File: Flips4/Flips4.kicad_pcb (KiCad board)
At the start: 2 copper layers, 21 x 59.1 mm, 7 parts, among them CN1 UFP2810, CN2 Conn_02x16_Counter_Clockwise, U1 FP2800A

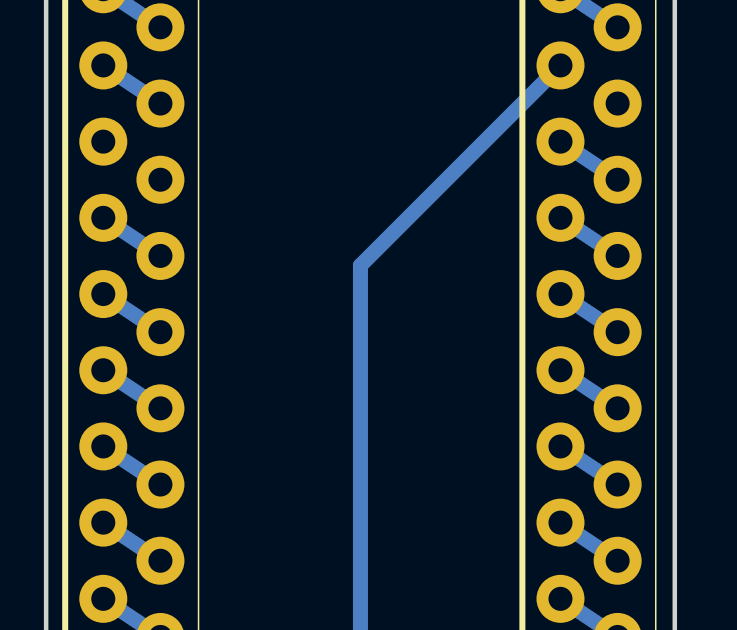
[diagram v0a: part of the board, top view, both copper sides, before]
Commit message: toggling copper behind "K" of "KiCad" logo
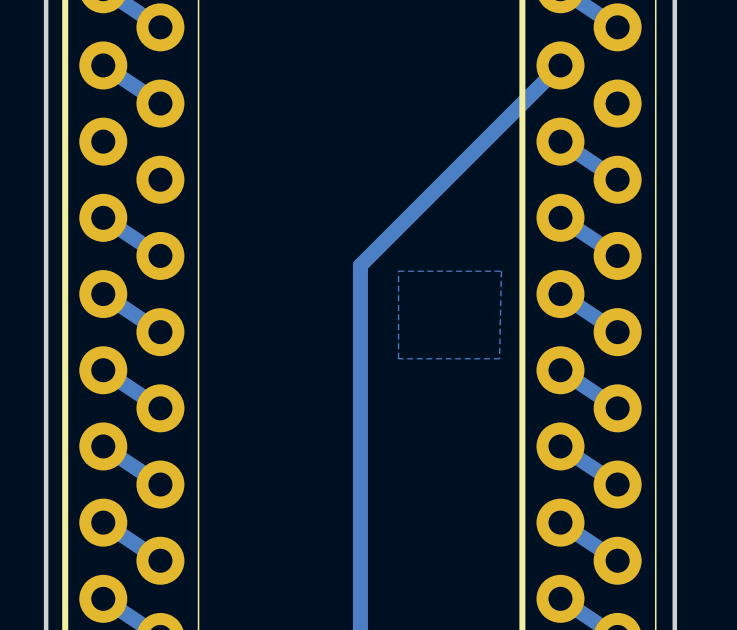
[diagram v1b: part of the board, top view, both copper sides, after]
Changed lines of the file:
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@@
+    )
+  )
+  (zone (net 0) (net_name "") (layer B.Cu) (hatch edge 0.508)
+    (connect_pads (clearance 0.1524))
+    (min_thickness 0.254)
+    (fill yes (arc_segments 16) (thermal_gap 0.508) (thermal_bridge_width 0.508))
+    (polygon
+      (pts
+        (xy 230.1875 86.233) (xy 233.6165 86.233) (xy 233.553 89.154) (xy 230.1875 89.154)
+      )
     )
   )

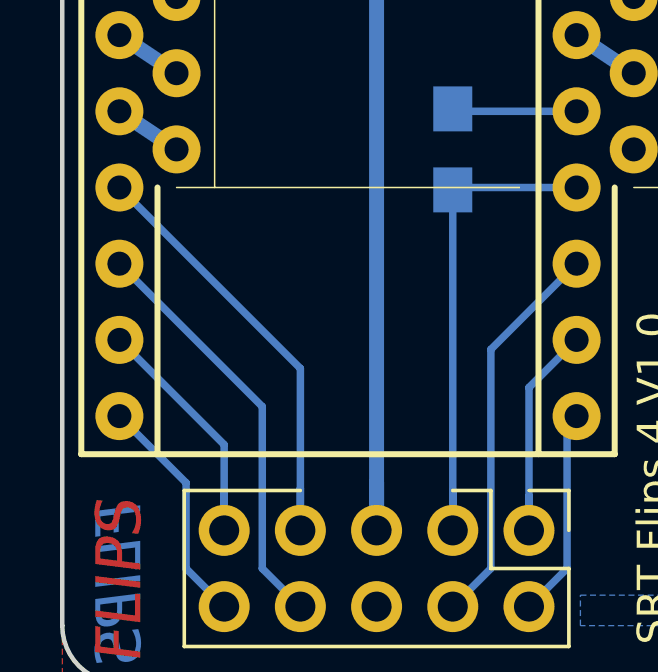
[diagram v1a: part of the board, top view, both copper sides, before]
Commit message: adding bypass capacitors
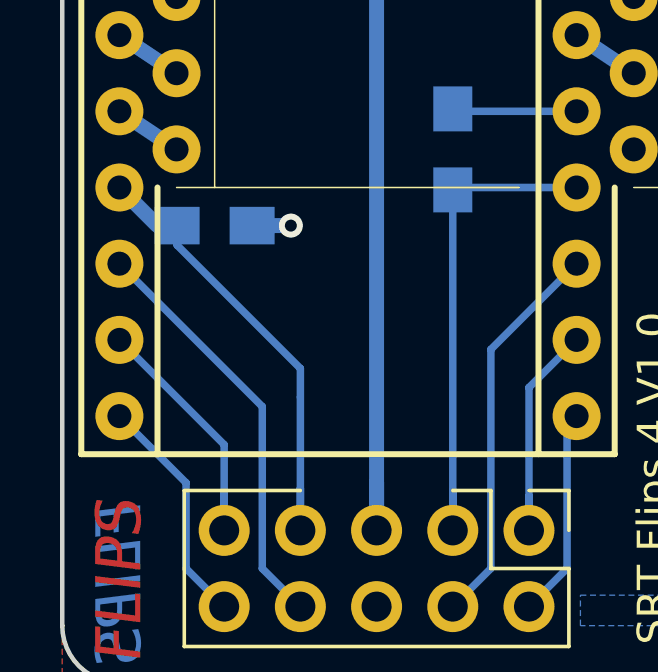
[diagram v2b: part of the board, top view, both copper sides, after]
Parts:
- added C1: 0U1, Capacitors_SMD:C_0805_HandSoldering, B.Cu at (223.5, 108.6)
- R1: value 10K/OPT -> 10K
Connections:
- CN2 pad 17: (no net) -> Net-(CN2-Pad17)
- CN2 pad 27: (no net) -> Net-(CN2-Pad27)
- CN2 pad 7: (no net) -> Net-(CN2-Pad7)
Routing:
- net GND: track 4.16 -> 5.45 mm, vias 0 -> 1
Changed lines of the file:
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@@
     (thickness 1.6)
     (drawings 35)
-    (tracks 64)
+    (tracks 70)
     (zones 0)
-    (modules 7)
-    (nets 40)
+    (modules 8)
+    (nets 43)
   )
   (page A4)
@@
   )
   (layers
-    (0 F.Cu signal hide)
+    (0 F.Cu signal)
     (31 B.Cu signal)
     (32 B.Adhes user)
@@
   (net 38 /A2)
   (net 39 /A0)
+  (net 40 "Net-(CN2-Pad27)")
+  (net 41 "Net-(CN2-Pad7)")
+  (net 42 "Net-(CN2-Pad17)")
   (net_class Default "Dies ist die voreingestellte Netzklasse."
     (clearance 0.2)
@@
     (add_net /Data)
     (add_net /Enable)
+    (add_net "Net-(CN2-Pad17)")
+    (add_net "Net-(CN2-Pad27)")
+    (add_net "Net-(CN2-Pad7)")
     (add_net VCC)
   )
@@
     (add_net "Net-(CN2-Pad8)")
     (add_net "Net-(CN2-Pad9)")
+  )
+  (module Capacitors_SMD:C_0805_HandSoldering (layer B.Cu)
+    (at 223.52 108.585)
+    (descr "Capacitor SMD 0805, hand soldering")
+    (tags "capacitor 0805")
+    (attr smd)
+    (fp_text reference C1 (at 0.635 2.54 90) (layer B.SilkS)
+      (effects (font (size 1 1) (thickness 0.15)) (justify mirror))
+    )
+    (fp_text value 0U1 (at -0.635 2.54 90) (layer B.SilkS)
+      (effects (font (size 1 1) (thickness 0.15)) (justify mirror))
+    )
+    (fp_line (start 2.25 -0.87) (end -2.25 -0.87) (layer B.CrtYd) (width 0.05))
+    (fp_line (start 2.25 -0.87) (end 2.25 0.88) (layer B.CrtYd) (width 0.05))
+    (fp_line (start -2.25 0.88) (end -2.25 -0.87) (layer B.CrtYd) (width 0.05))
+    (fp_line (start -2.25 0.88) (end 2.25 0.88) (layer B.CrtYd) (width 0.05))
+    (fp_line (start -0.5 -0.85) (end 0.5 -0.85) (layer B.SilkS) (width 0.12))
+    (fp_line (start 0.5 0.85) (end -0.5 0.85) (layer B.SilkS) (width 0.12))
+    (fp_line (start -1 0.62) (end 1 0.62) (layer B.Fab) (width 0.1))
+    (fp_line (start 1 0.62) (end 1 -0.62) (layer B.Fab) (width 0.1))
+    (fp_line (start 1 -0.62) (end -1 -0.62) (layer B.Fab) (width 0.1))
+    (fp_line (start -1 -0.62) (end -1 0.62) (layer B.Fab) (width 0.1))
+    (fp_text user %R (at 0 1.75) (layer B.Fab)
+      (effects (font (size 1 1) (thickness 0.15)) (justify mirror))
+    )
+    (pad 2 smd rect (at 1.25 0) (size 1.5 1.25) (layers B.Cu B.Paste B.Mask)
+      (net 30 GND))
+    (pad 1 smd rect (at -1.25 0) (size 1.5 1.25) (layers B.Cu B.Paste B.Mask)
+      (net 31 VCC))
+    (model Capacitors_SMD.3dshapes/C_0805.wrl
+      (at (xyz 0 0 0))
+      (scale (xyz 1 1 1))
+      (rotate (xyz 0 0 0))
+    )
   )
   (module Own:Pin_Header_Angle_Shrouded_2x05_Pitch2.54mm (layer F.Cu)
@@
     (pad 12 thru_hole oval (at 0 27.94) (size 1.6 1.6) (drill 0.8) (layers *.Cu *.Mask)
       (net 9 "Net-(CN2-Pad12)"))
-    (pad 27 thru_hole oval (at 15.24 12.7) (size 1.6 1.6) (drill 0.8) (layers *.Cu *.Mask))
+    (pad 27 thru_hole oval (at 15.24 12.7) (size 1.6 1.6) (drill 0.8) (layers *.Cu *.Mask)
+      (net 40 "Net-(CN2-Pad27)"))
     (pad 11 thru_hole oval (at 0 25.4) (size 1.6 1.6) (drill 0.8) (layers *.Cu *.Mask)
       (net 11 "Net-(CN2-Pad11)"))
@@
     (pad 23 thru_hole oval (at 15.24 22.86) (size 1.6 1.6) (drill 0.8) (layers *.Cu *.Mask)
       (net 24 "Net-(CN2-Pad23)"))
-    (pad 7 thru_hole oval (at 0 15.24) (size 1.6 1.6) (drill 0.8) (layers *.Cu *.Mask))
+    (pad 7 thru_hole oval (at 0 15.24) (size 1.6 1.6) (drill 0.8) (layers *.Cu *.Mask)
+      (net 41 "Net-(CN2-Pad7)"))
     (pad 22 thru_hole oval (at 15.24 25.4) (size 1.6 1.6) (drill 0.8) (layers *.Cu *.Mask)
       (net 26 "Net-(CN2-Pad22)"))
@@
     (pad 2 thru_hole oval (at 0 2.54) (size 1.6 1.6) (drill 0.8) (layers *.Cu *.Mask)
       (net 27 "Net-(CN2-Pad2)"))
-    (pad 17 thru_hole oval (at 15.24 38.1) (size 1.6 1.6) (drill 0.8) (layers *.Cu *.Mask))
+    (pad 17 thru_hole oval (at 15.24 38.1) (size 1.6 1.6) (drill 0.8) (layers *.Cu *.Mask)
+      (net 42 "Net-(CN2-Pad17)"))
     (pad 1 thru_hole circle (at 0 0) (size 1.6 1.6) (drill 0.8) (layers *.Cu *.Mask)
       (net 29 "Net-(CN2-Pad1)"))
@@
       (effects (font (size 1 1) (thickness 0.15)) (justify mirror))
     )
-    (fp_text value 10K/OPT (at 0 -1.75 90) (layer B.SilkS)
+    (fp_text value 10K (at 0 -1.75 90) (layer B.SilkS)
       (effects (font (size 1 1) (thickness 0.15)) (justify mirror))
     )
@@
   (segment (start 231.5375 104.775) (end 231.4575 104.695) (width 0.5) (layer B.Cu) (net 30) (status 30))
   (segment (start 235.585 104.775) (end 231.5375 104.775) (width 0.25) (layer B.Cu) (net 30) (status 30))
-  (segment (start 220.345 107.315) (end 226.3775 113.3475) (width 0.25) (layer B.Cu) (net 31) (status 400010))
-  (segment (start 226.3775 113.3475) (end 226.3775 117.348) (width 0.25) (layer B.Cu) (net 31))
+  (via (at 226.06 108.585) (size 0.8) (drill 0.4) (layers F.Cu B.Cu) (net 30))
+  (segment (start 224.77 108.585) (end 226.06 108.585) (width 0.5) (layer B.Cu) (net 30) (status 400010))
   (segment (start 226.3775 117.348) (end 226.3775 118.11) (width 0.25) (layer B.Cu) (net 31) (status 800020))
   (segment (start 226.3775 118.745) (end 226.3775 117.348) (width 0.25) (layer B.Cu) (net 31) (status 400010))
+  (segment (start 226.3775 114.3) (end 226.3775 117.348) (width 0.25) (layer B.Cu) (net 31))
+  (segment (start 222.27 108.585) (end 221.615 108.585) (width 0.25) (layer B.Cu) (net 31) (status C00000))
+  (segment (start 221.615 108.585) (end 220.345 107.315) (width 0.5) (layer B.Cu) (net 31) (status C00000))
+  (segment (start 226.3775 114.3) (end 226.3775 113.3475) (width 0.25) (layer B.Cu) (net 31))
+  (segment (start 226.3775 113.3475) (end 222.27 109.24) (width 0.25) (layer B.Cu) (net 31))
+  (segment (start 222.27 109.24) (end 222.27 108.585) (width 0.25) (layer B.Cu) (net 31) (status 800000))
   (segment (start 235.585 79.375) (end 228.9175 86.0425) (width 0.5) (layer B.Cu) (net 32) (status 10))
   (segment (start 228.9175 86.0425) (end 228.9175 117.1575) (width 0.5) (layer B.Cu) (net 32))

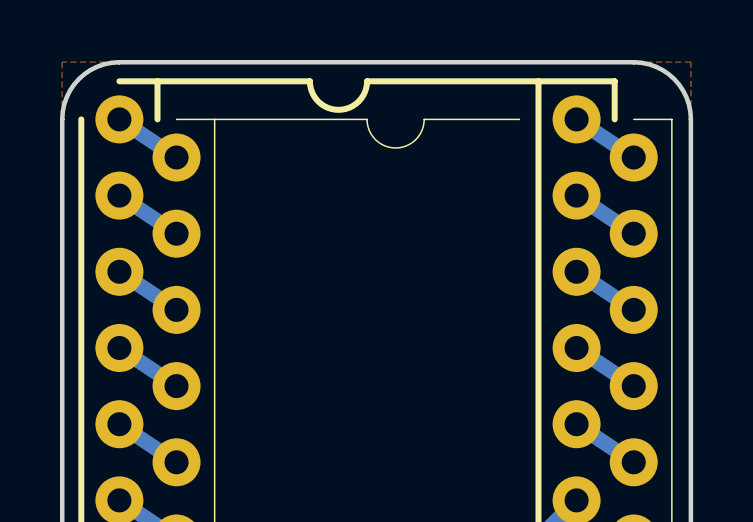
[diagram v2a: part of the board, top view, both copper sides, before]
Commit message: More FP2800 info printed on Flips4
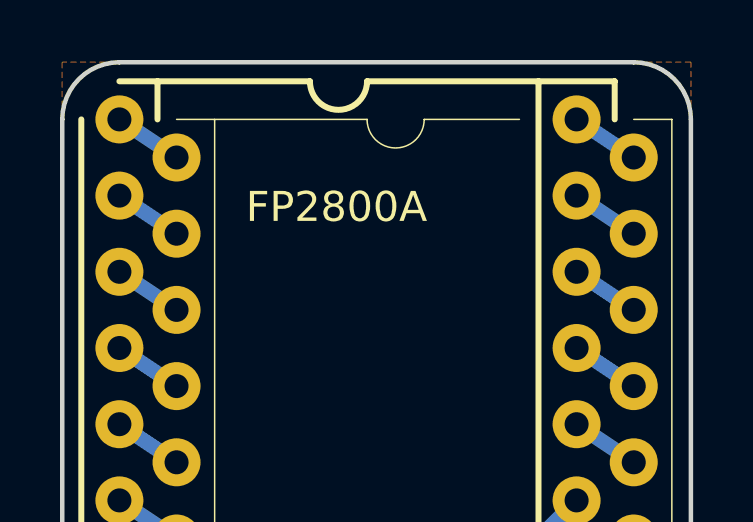
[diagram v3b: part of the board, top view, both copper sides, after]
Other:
- board text added: "SRT Flips 4 V1.0 2018-11-03 github.com/cawapy/FlipSuite Remote FP2800"
- board text removed: "SRT Flips 4 V1.0 2018-11-03 github.com/cawapy/FlipSuite"
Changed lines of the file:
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@@
       (effects (font (size 1 1) (thickness 0.15)))
     )
-    (fp_text value FP2800A (at 8.255 3.81) (layer F.Fab)
+    (fp_text value FP2800A (at 7.239 2.921) (layer F.SilkS)
       (effects (font (size 1 1) (thickness 0.15)))
     )
@@
   (gr_line (start 239.395 121.92) (end 239.395 66.675) (angle 90) (layer Edge.Cuts) (width 0.15))
   (gr_line (start 220.345 123.825) (end 237.49 123.825) (angle 90) (layer Edge.Cuts) (width 0.15))
-  (gr_text "SRT Flips 4 V1.0 2018-11-03\ngithub.com/cawapy/FlipSuite" (at 226.06 67.31 90) (layer B.SilkS)
+  (gr_text "SRT Flips 4 V1.0 2018-11-03\ngithub.com/cawapy/FlipSuite\nRemote\nFP2800" (at 228.6 67.31 90) (layer B.SilkS)
     (effects (font (size 1.5 1.5) (thickness 0.3)) (justify left mirror))
   )

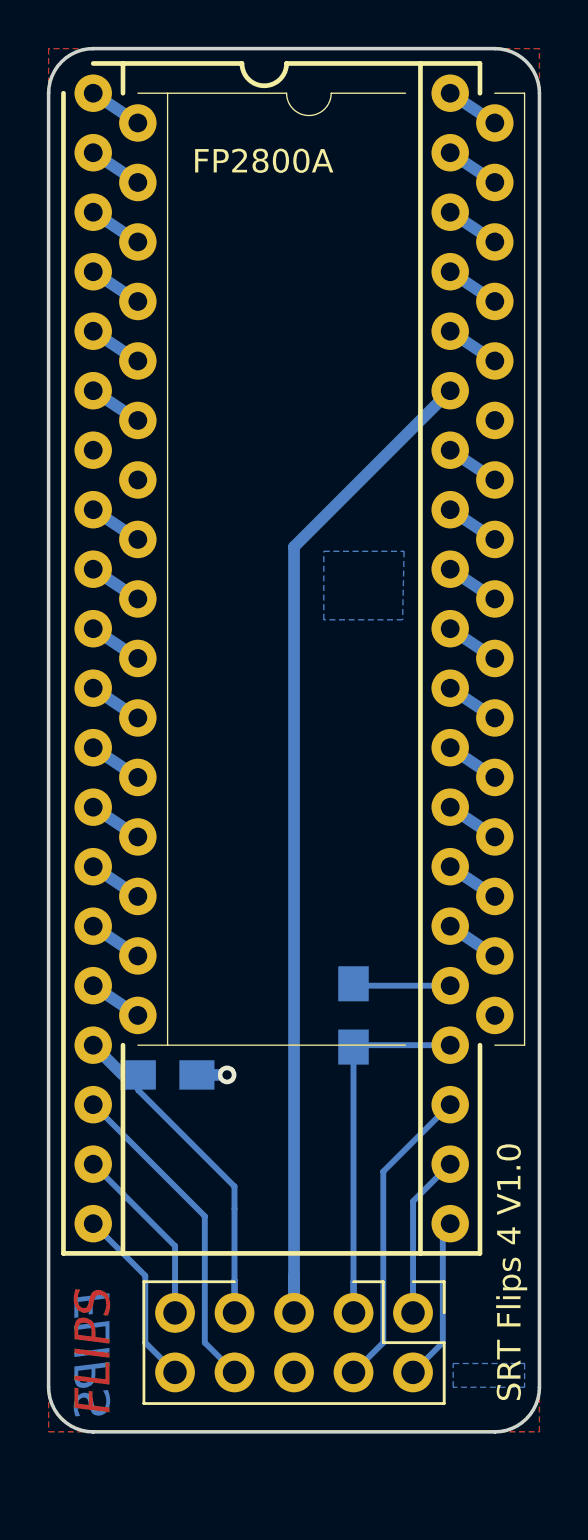
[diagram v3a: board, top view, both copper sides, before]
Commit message: Using straight instead of angled IDC connector due to limited space on Brose display
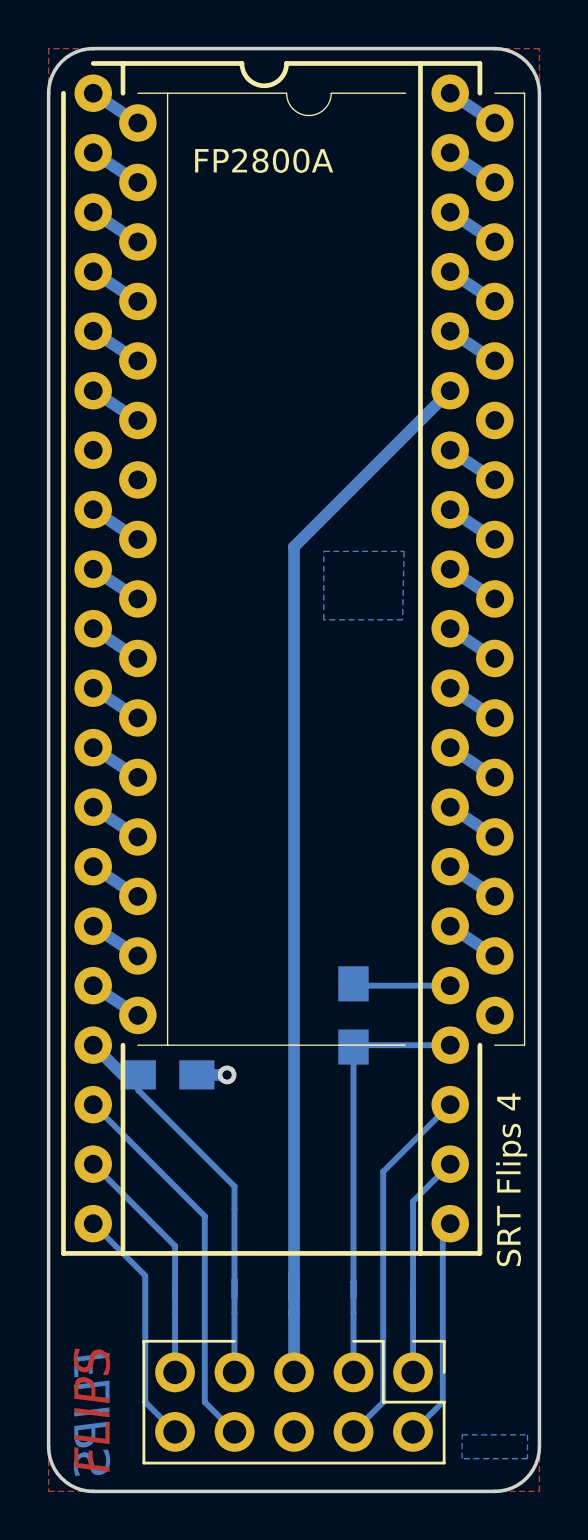
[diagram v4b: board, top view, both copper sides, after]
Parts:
- CN1: footprint Own:Pin_Header_Angle_Shrouded_2x05_Pitch2.54mm -> Own:Pin_Header_Straight_Shrouded_2x05_Pitch2.54mm
- moved REF*** 2.73 mm to (229.9, 116.2)
- moved CN1 2.54 mm to (234.0, 121.3)
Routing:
- net /A2: track 7.80 -> 10.3 mm
- net /Data: track 13.1 -> 15.7 mm
- net /B0: track 7.01 -> 9.55 mm
- net /A1: track 13.9 -> 16.5 mm
- net /B1: track 7.52 -> 10.1 mm
- net VCC: track 15.1 -> 17.6 mm
- net /Enable: track 16.3 -> 18.8 mm
- net /A0: track 8.37 -> 10.9 mm
- net +12V: track 43.1 -> 45.6 mm
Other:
- board size 21 x 59.1 mm -> 21 x 61.6 mm
- board text added: "SRT Flips 4"
- board text added: "Space on Brose 9923 BR3/70.28/19"
- board text removed: "SRT Flips 4 V1.0"
